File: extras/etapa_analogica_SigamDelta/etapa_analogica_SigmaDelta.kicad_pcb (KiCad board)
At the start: 2 copper layers, 63.5 x 78.8 mm, 17 parts, among them P1 CONN_02X10, P2 CONN_01X03, P3 CONN_02X10, P4 BNC

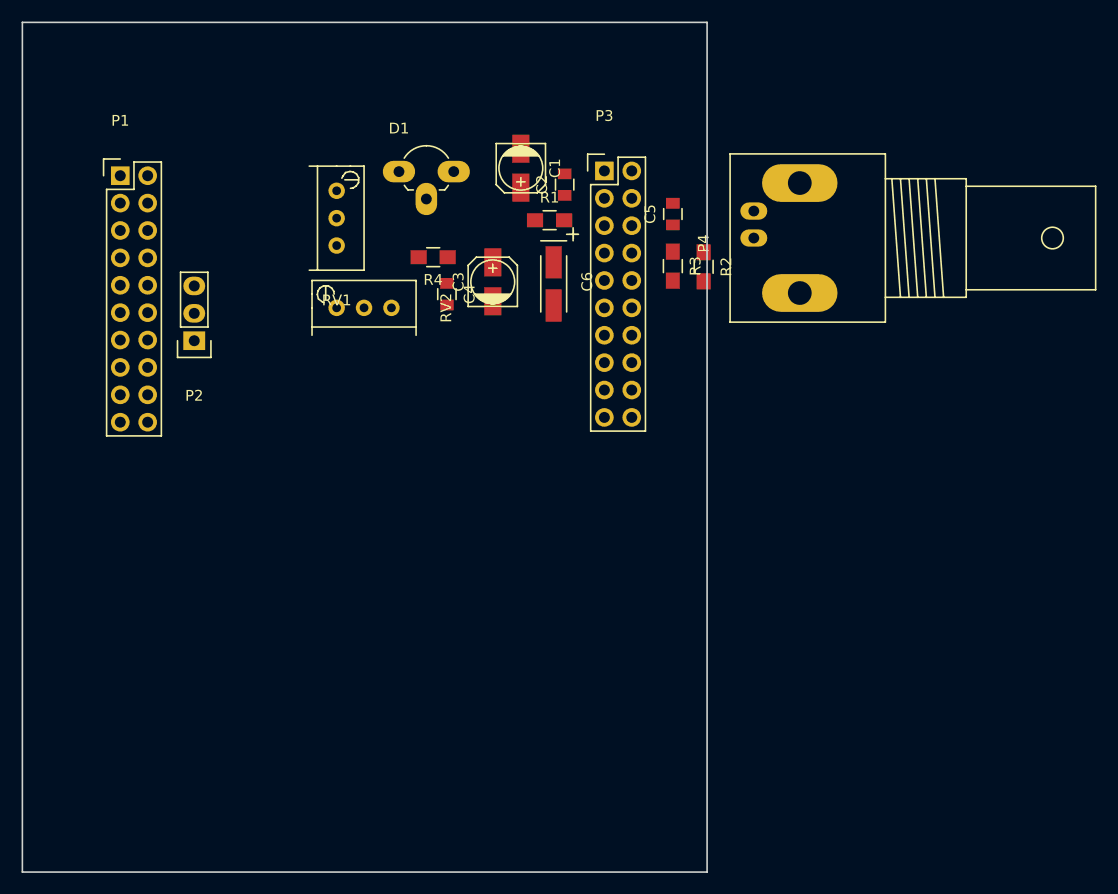
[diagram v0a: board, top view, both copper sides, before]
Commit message: Revert "Starting the layout"
This reverts commit 84db6e4c9a3b0a09193008fcb0844fcb533dafef.
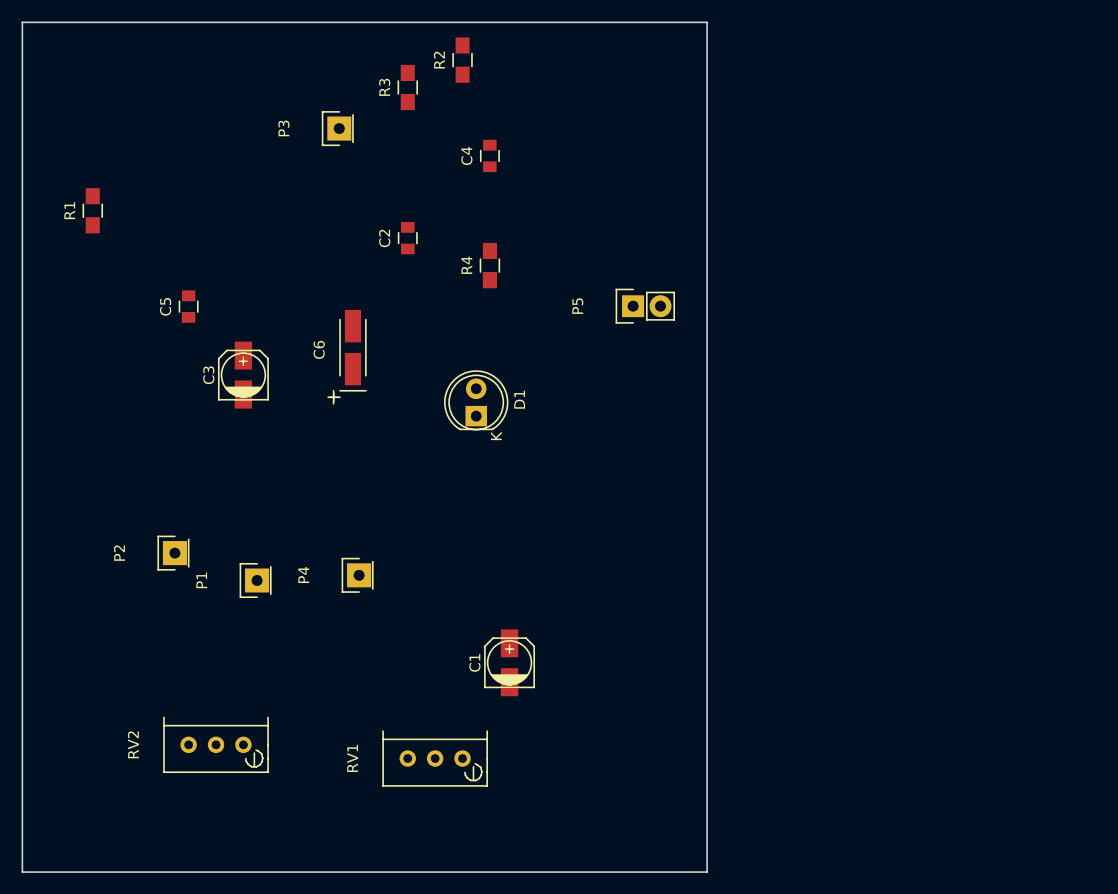
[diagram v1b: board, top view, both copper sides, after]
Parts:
- added P5: CONN_01X02, Pin_Headers:Pin_Header_Straight_1x02, F.Cu at (143.0, 82.1)
- D1: footprint Housings_TO-92:TO-92_Rugged_Reverse -> LEDs:LED-5MM
- P1, P3: value CONN_02X10 -> CONN_01X01; footprint Pin_Headers:Pin_Header_Straight_2x10 -> Pin_Headers:Pin_Header_Straight_1x01
- P2: value CONN_01X03 -> CONN_01X01; footprint Pin_Headers:Pin_Header_Straight_1x03 -> Pin_Headers:Pin_Header_Straight_1x01
- P4: value BNC -> CONN_01X01; footprint Sockets_BNC:BNC_Socket_TYCO-AMP_LargePads -> Pin_Headers:Pin_Header_Straight_1x01
- RV2: value 10k -> 1k
- moved RV1 53.9 mm to (127.2, 124.1), turned to 90 degrees
- moved P4 52.1 mm to (117.6, 107.1), turned to 90 degrees
- moved C1 45.9 mm to (131.5, 115.2), turned to 90 degrees
- moved C5 45.7 mm to (101.8, 82.2)
- moved R1 42.4 mm to (92.9, 73.3), turned to 90 degrees
- moved RV2 41.4 mm to (106.9, 122.8), turned to 90 degrees
- moved P1 39.6 mm to (108.1, 107.6), turned to 90 degrees
- moved R3 29.6 mm to (122.1, 61.9), turned to 90 degrees
- moved R2 29.5 mm to (127.2, 59.3), turned to 90 degrees
- moved P3 24.9 mm to (115.8, 65.7), turned to 90 degrees
- moved C3 24.7 mm to (106.9, 88.5)
- moved D1 23.8 mm to (128.4, 92.3), turned to 90 degrees
- moved P2 19.8 mm to (100.5, 105.0), turned to 90 degrees
- moved C6 19.5 mm to (117.0, 86.0), turned to 90 degrees
- moved C2 15.4 mm to (122.1, 75.8)
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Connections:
- C1 pad 1: /3,3v -> Vcc
- C2 pad 1: /3,3v -> Vcc
- C3 pad 1: /N40 -> Vref
- C4 pad 1: /N40 -> Vref
- C5 pad 1: /P41 -> Vin
- C6 pad 1: /N40 -> Vref
- D1 pad 1: GND -> Net-(D1-Pad1)
- D1 pad 2: Net-(D1-Pad2) -> GND
- P1 pad 1: Net-(P1-Pad1) -> Vsignal
- P2 pad 1: /Tx -> GND
- P3 pad 1: Net-(P3-Pad1) -> Vfb
- P4 pad 1: Net-(P4-Pad1) -> Vcc
- R1 pad 1: Net-(D1-Pad2) -> Net-(D1-Pad1)
- R1 pad 2: /3,3v -> Vcc
- R2 pad 1: /P41 -> Vin
- R2 pad 2: Net-(P4-Pad1) -> Vsignal
- R3 pad 1: /P41 -> Vin
- R3 pad 2: /P35 -> Vfb
- R4 pad 1: /N40 -> Vref
- RV1 pad 1: Net-(D1-Pad2) -> Net-(D1-Pad1)
- RV1 pad 2: Net-(RV1-Pad2) -> Net-(R4-Pad2)
- RV1 pad 3: Net-(RV1-Pad2) -> Net-(RV1-Pad3)
- RV2 pad 1: Net-(RV1-Pad2) -> Net-(RV1-Pad3)
- RV2 pad 2: Net-(R4-Pad2) -> GND

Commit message: Starting the layout
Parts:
- removed P5: CONN_01X02, Pin_Headers:Pin_Header_Straight_1x02
- D1: footprint LEDs:LED-5MM -> Housings_TO-92:TO-92_Rugged_Reverse
- P1, P3: value CONN_01X01 -> CONN_02X10; footprint Pin_Headers:Pin_Header_Straight_1x01 -> Pin_Headers:Pin_Header_Straight_2x10
- P2: value CONN_01X01 -> CONN_01X03; footprint Pin_Headers:Pin_Header_Straight_1x01 -> Pin_Headers:Pin_Header_Straight_1x03
- P4: value CONN_01X01 -> BNC; footprint Pin_Headers:Pin_Header_Straight_1x01 -> Sockets_BNC:BNC_Socket_TYCO-AMP_LargePads
- RV2: value 1k -> 10k
- moved RV1 53.9 mm to (115.5, 71.4), turned to 180 degrees
- moved P4 52.1 mm to (159.2, 75.8), turned to 270 degrees
- moved C1 45.9 mm to (132.6, 69.3), turned to 270 degrees
- moved C5 45.7 mm to (146.7, 73.6)
- moved R1 42.4 mm to (135.3, 74.2), turned to 0 degrees
- moved RV2 41.4 mm to (115.5, 82.3), turned to 270 degrees
- moved P1 39.6 mm to (95.4, 70.0), turned to 0 degrees
- moved R3 29.6 mm to (146.7, 78.4), turned to 270 degrees
- moved R2 29.5 mm to (149.5, 78.5), turned to 270 degrees
- moved P3 24.9 mm to (140.3, 69.6), turned to 0 degrees
- moved C3 24.7 mm to (130.0, 79.9)
- moved D1 23.8 mm to (121.3, 69.7), turned to 0 degrees
- moved P2 19.8 mm to (102.3, 85.3), turned to 180 degrees
- moved C6 19.5 mm to (135.6, 80.1), turned to 270 degrees
- moved C2 15.4 mm to (136.7, 70.9)
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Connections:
- C1 pad 1: Vcc -> /3,3v
- C2 pad 1: Vcc -> /3,3v
- C3 pad 1: Vref -> /N40
- C4 pad 1: Vref -> /N40
- C5 pad 1: Vin -> /P41
- C6 pad 1: Vref -> /N40
- D1 pad 1: Net-(D1-Pad1) -> GND
- D1 pad 2: GND -> Net-(D1-Pad2)
- P1 pad 1: Vsignal -> Net-(P1-Pad1)
- P2 pad 1: GND -> /Tx
- P3 pad 1: Vfb -> Net-(P3-Pad1)
- P4 pad 1: Vcc -> Net-(P4-Pad1)
- R1 pad 1: Net-(D1-Pad1) -> Net-(D1-Pad2)
- R1 pad 2: Vcc -> /3,3v
- R2 pad 1: Vin -> /P41
- R2 pad 2: Vsignal -> Net-(P4-Pad1)
- R3 pad 1: Vin -> /P41
- R3 pad 2: Vfb -> /P35
- R4 pad 1: Vref -> /N40
- RV1 pad 1: Net-(D1-Pad1) -> Net-(D1-Pad2)
- RV1 pad 2: Net-(R4-Pad2) -> Net-(RV1-Pad2)
- RV1 pad 3: Net-(RV1-Pad3) -> Net-(RV1-Pad2)
- RV2 pad 1: Net-(RV1-Pad3) -> Net-(RV1-Pad2)
- RV2 pad 2: GND -> Net-(R4-Pad2)
